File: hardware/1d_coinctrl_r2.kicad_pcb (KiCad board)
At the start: 2 copper layers, 158.8 x 158.8 mm, 99 parts, among them J1 +12V INPUT, J10 USB_B, J2 CO LINE, J3 V_RLY_SEL, J4 TEL LINE, J5 COIN LINE, J6 DB9_Female_MountingHoles, J7 Conn_01x02, J8 Conn_02x10_Odd_Even, J9 Conn_01x06_Male, K1 G5V-2-DC12, K10 L4_COIN_CTRL, K11 G5V-2-DC12, K2 G5V-2-DC12, K3 L1_HOLD, K4 L1_COIN_CTRL, K5 L2_HOLD, K6 L2_COIN_CTRL, K7 L3_HOLD, K8 L3_COIN_CTRL, K9 L4_HOLD, SW1 SW_Push, U10 H11AA1, U14 MAX202, U2 V7805-1000, U3 PIC18F4550-IP, U4 74LS06, U5 74LS06, U6 H11AA1, U7 H11AA1, U8 H11AA1, U9 H11AA1

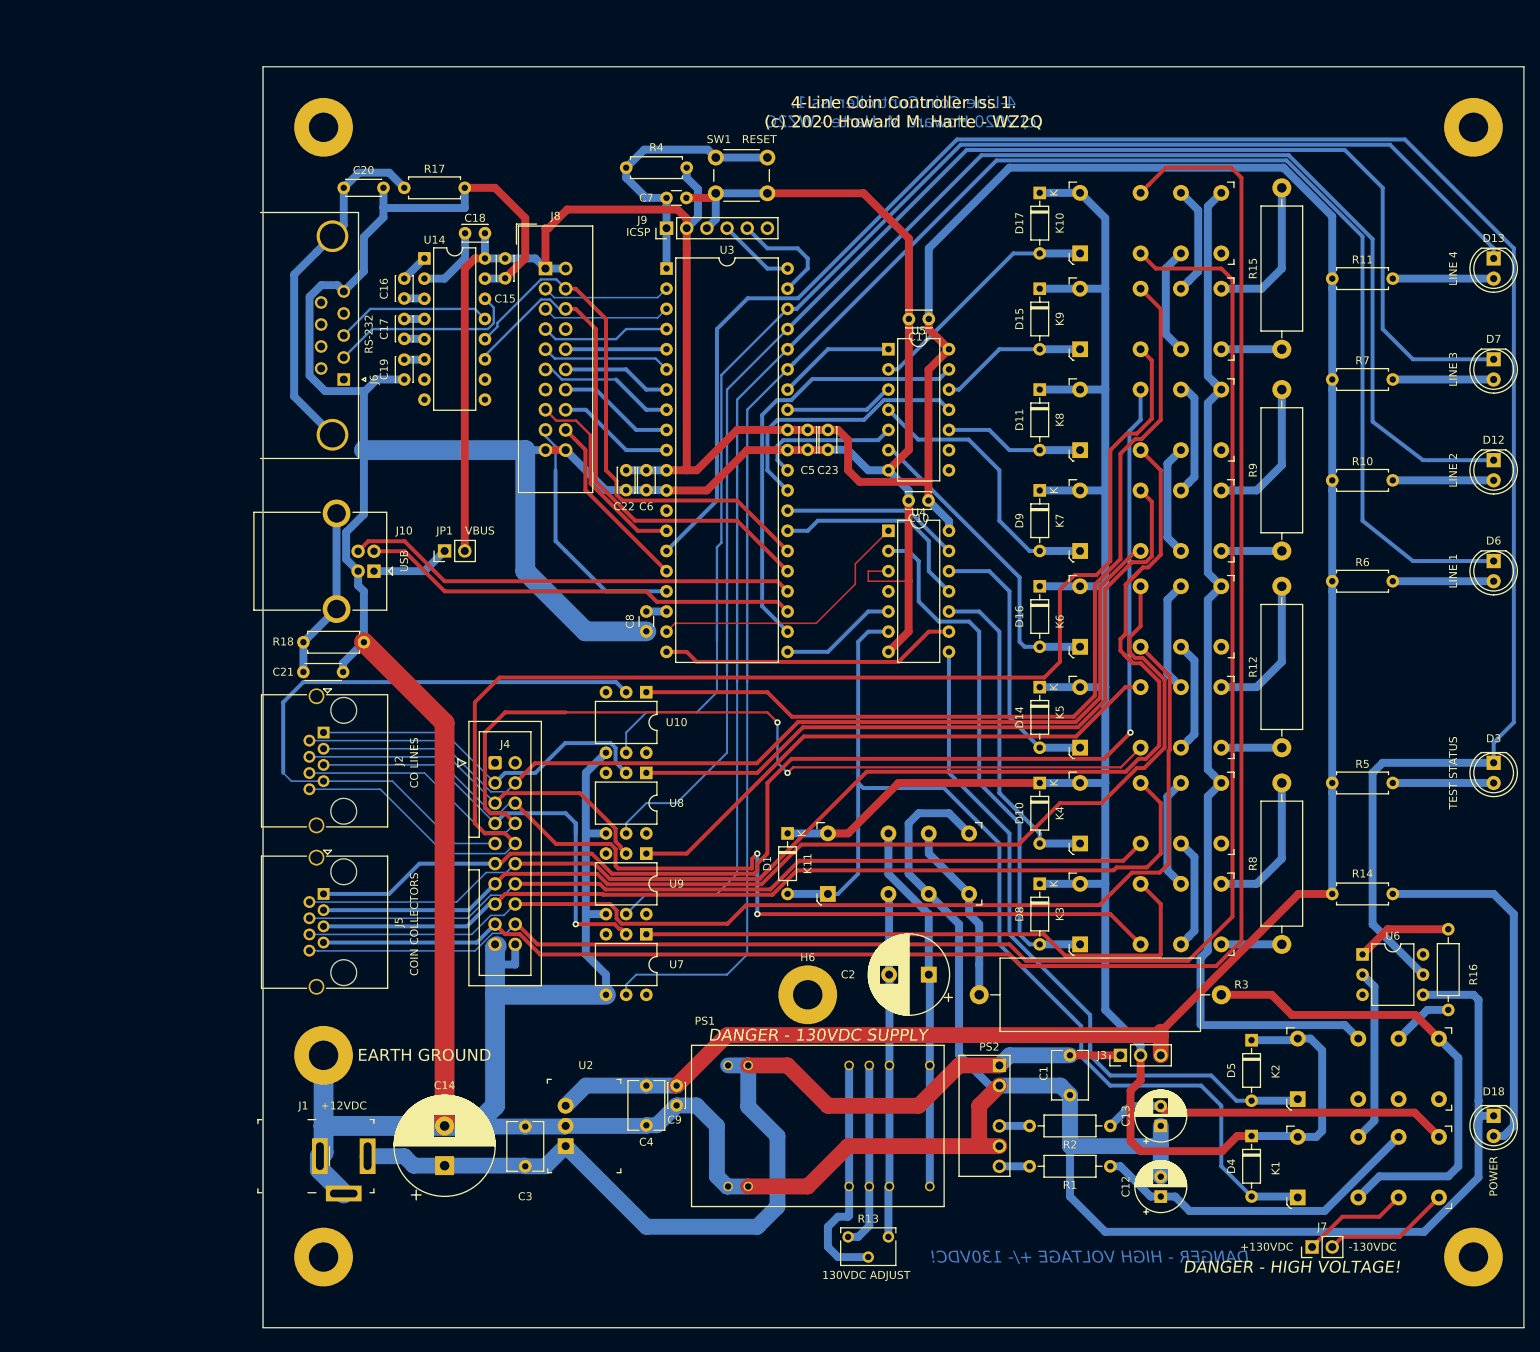
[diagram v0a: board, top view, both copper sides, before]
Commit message: Issue 2 schmatic and Layout
Added polarity reversal detection to monitor answer supervision.
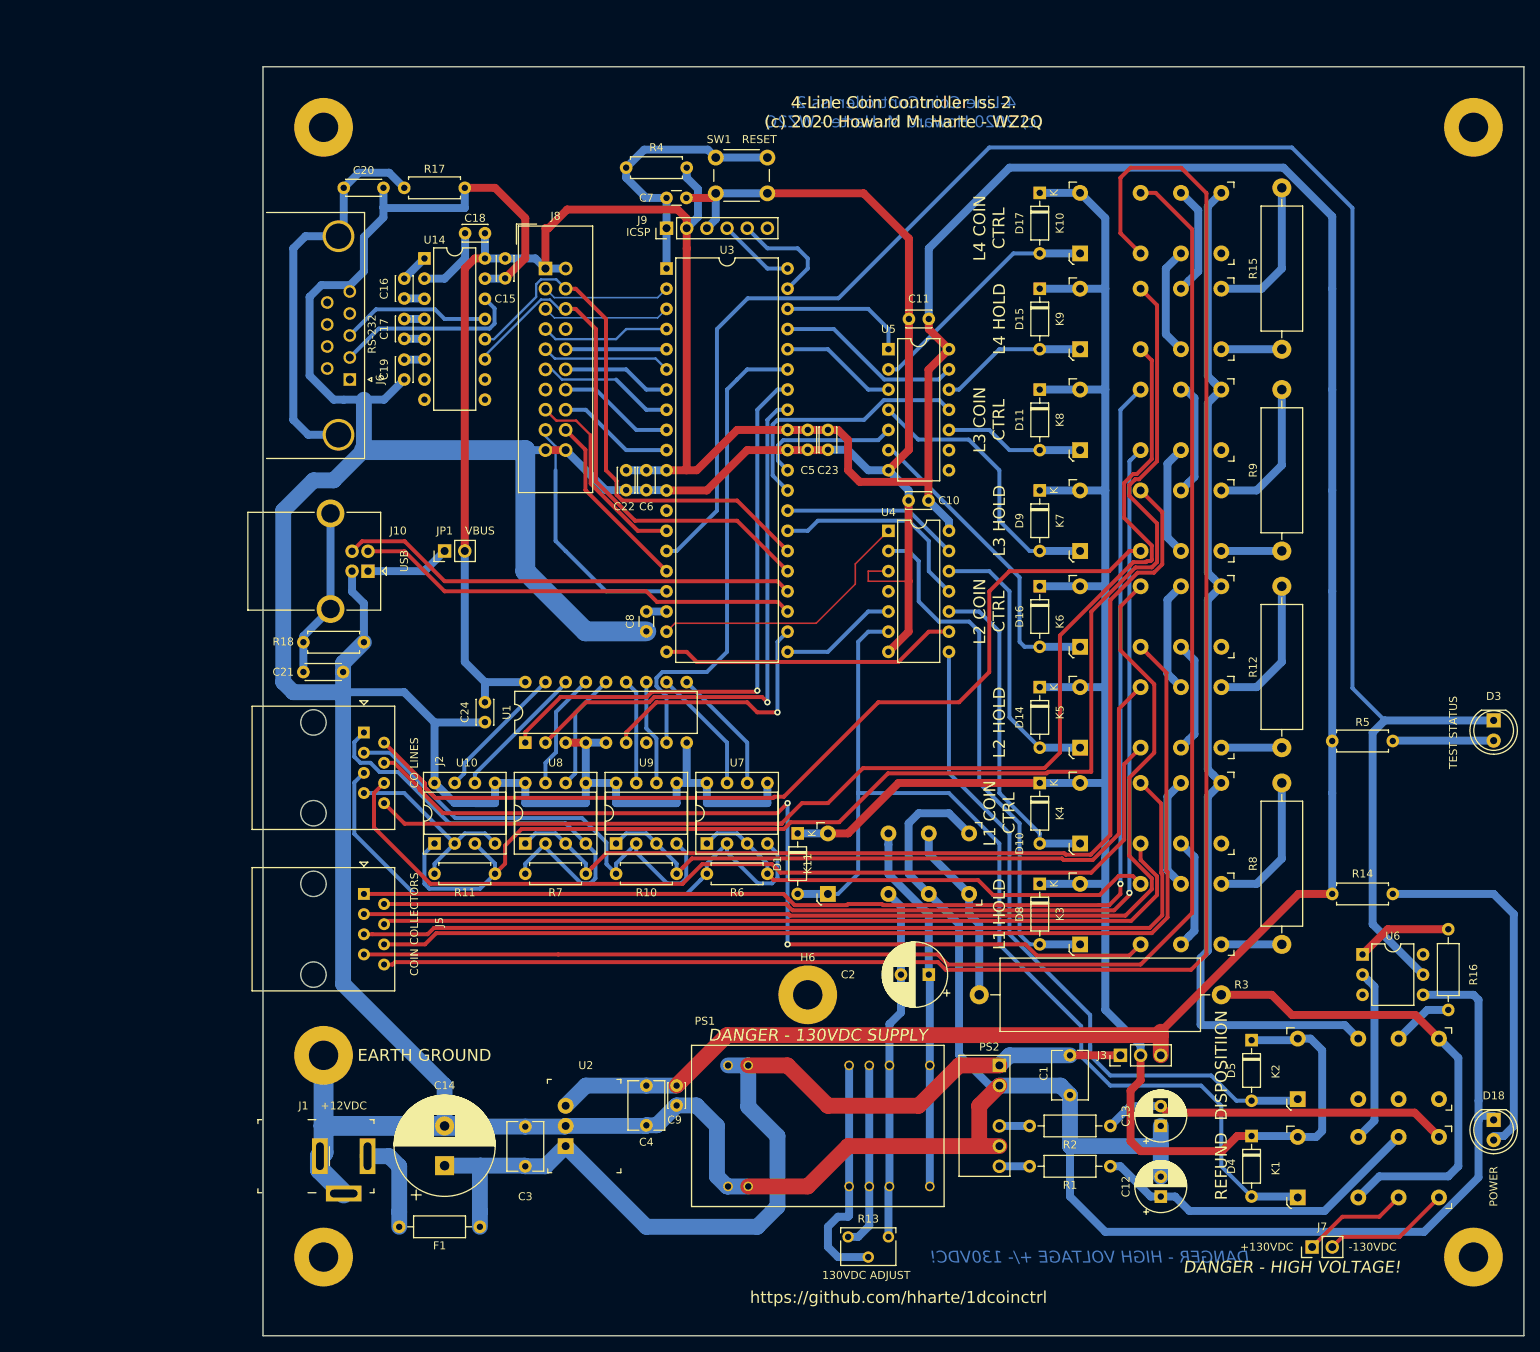
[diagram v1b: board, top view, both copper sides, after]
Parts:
- removed D12, D13, D6, D7: LED, LED_THT:LED_D5.0mm
- removed J4: TEL LINE, Connector_IDC:IDC-Header_2x10_P2.54mm_Vertical
- added C24: 0.1uF, Capacitor_THT:C_Disc_D3.0mm_W2.0mm_P2.50mm, F.Cu at (111.8, 100.3)
- added F1: Fuse, Resistor_THT:R_Axial_DIN0207_L6.3mm_D2.5mm_P10.16mm_Horizontal, F.Cu at (111.1, 166.4)
- added U1: MCP23008-xP, Package_DIP:DIP-18_W7.62mm, F.Cu at (116.8, 105.4)
- C2: footprint Capacitor_THT:CP_Radial_D10.0mm_P5.00mm -> Capacitor_THT:CP_Radial_D8.0mm_P3.50mm
- J2, J5: footprint Connector_RJ:RJ45_Amphenol_RJHSE5380 -> Connector_RJ:RJ45_Amphenol_54602-x08_Horizontal
- R10, R11, R6, R7: value 220 -> 120
- U10, U7, U8, U9: value H11AA1 -> ILD74; footprint Package_DIP:DIP-6_W7.62mm -> Package_DIP:DIP-8_W7.62mm_Socket
- moved R11 129.3 mm to (113.0, 121.9), turned to 180 degrees
- moved R7 112.7 mm to (124.5, 121.9), turned to 180 degrees
- moved R10 96.3 mm to (135.9, 121.9), turned to 180 degrees
- moved R6 80.1 mm to (147.3, 121.9), turned to 180 degrees
- moved U10 32.8 mm to (105.4, 118.1), turned to 90 degrees
- moved U8 17.6 mm to (116.8, 118.1), turned to 90 degrees
- moved U7 13.7 mm to (139.7, 118.1), turned to 90 degrees
- moved D3 5.33 mm to (238.8, 102.6)
- moved R5 5.28 mm to (218.4, 105.2)
- moved J2 5.08 mm to (96.5, 104.1)
- moved J5 5.08 mm to (96.5, 124.5)
- moved U9 4.02 mm to (128.3, 118.1), turned to 90 degrees
- moved D1 1.27 mm to (151.1, 116.8)
- moved J10 0.76 mm to (97.0, 83.8)
- moved J6 0.76 mm to (94.7, 59.7)
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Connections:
- net /GPIO/RD3_DISPOSITION renamed /GPIO/RD1_DISPOSITION
- net /GPIO/RE0_L3_COIN_CONTROL renamed /GPIO/RD6_L3_COIN_CONTROL
- J1 pad 1: +12V -> Net-(F1-Pad2)
- J6 pad 1: Net-(J6-Pad1) -> (no net)
- J6 pad 4: Net-(J6-Pad4) -> (no net)
- J6 pad 6: Net-(J6-Pad6) -> (no net)
- J6 pad 7: Net-(J6-Pad7) -> (no net)
- J6 pad 8: Net-(J6-Pad8) -> (no net)
- J6 pad 9: Net-(J6-Pad9) -> (no net)
- J8 pad 13: Net-(J8-Pad13) -> (no net)
- J8 pad 8: Net-(J8-Pad8) -> (no net)
- J9 pad 6: Net-(J9-Pad6) -> (no net)
- K10 pad 8: Net-(K10-Pad8) -> (no net)
- K2 pad 4: Net-(K2-Pad4) -> (no net)
- K2 pad 6: Net-(K2-Pad6) -> (no net)
- K2 pad 8: Net-(K2-Pad8) -> (no net)
- K4 pad 8: Net-(K4-Pad8) -> (no net)
- K6 pad 8: Net-(K6-Pad8) -> (no net)
- K8 pad 8: Net-(K8-Pad8) -> (no net)
- R10 pad 1: +5V -> Net-(K5-Pad13)
- R10 pad 2: Net-(D12-Pad2) -> /L2_CO_TIP
- R11 pad 1: +5V -> Net-(K9-Pad13)
- R11 pad 2: Net-(D13-Pad2) -> /L4_CO_TIP
- R6 pad 1: +5V -> Net-(K3-Pad13)
- R6 pad 2: Net-(D6-Pad2) -> /L1_CO_TIP
- R7 pad 1: +5V -> Net-(K7-Pad13)
- R7 pad 2: Net-(D7-Pad2) -> /L3_CO_TIP
- U10 pad 3: Net-(U10-Pad3) -> Net-(K9-Pad13)
- U10 pad 4: GND -> /L4_CO_TIP
- U10 pad 5: /GPIO/L4_OFF_HOOK -> GND
- U10 pad 6: Net-(U10-Pad6) -> /Coin Line Control/L4_OFF_HOOK_F
- U14 pad 10: Net-(U14-Pad10) -> (no net)
- U14 pad 7: Net-(U14-Pad7) -> (no net)
- U14 pad 8: Net-(U14-Pad8) -> (no net)
- U14 pad 9: Net-(U14-Pad9) -> (no net)
- U3 pad 13: Net-(U3-Pad13) -> (no net)
- U3 pad 22: /GPIO/RD6_L4_HOLD_CO -> /GPIO/I2C_RESET
- U3 pad 33: /GPIO/RB0_L3_HOLD_CO -> /GPIO/I2C_SDA
- U3 pad 34: /GPIO/RB1_L4_COIN_CONTROL -> /GPIO/I2C_SCL
- U3 pad 35: /GPIO/L1_OFF_HOOK -> /GPIO/I2C_INT
- U3 pad 36: /GPIO/L2_OFF_HOOK -> /GPIO/RB3_L3_HOLD_CO
- U3 pad 37: /GPIO/L3_OFF_HOOK -> /GPIO/RB4_L4_HOLD_CO
- U3 pad 38: /GPIO/L4_OFF_HOOK -> /GPIO/RB1_L4_COIN_CONTROL
- U4 pad 4: Net-(U4-Pad4) -> (no net)
- U5 pad 13: /GPIO/RD6_L4_HOLD_CO -> /GPIO/RB4_L4_HOLD_CO
- U5 pad 3: /GPIO/RB0_L3_HOLD_CO -> /GPIO/RB3_L3_HOLD_CO
- U6 pad 3: Net-(U6-Pad3) -> (no net)
- U6 pad 6: Net-(U6-Pad6) -> (no net)
- U7 pad 3: Net-(U7-Pad3) -> Net-(K3-Pad13)
- U7 pad 4: GND -> /L1_CO_TIP
- U7 pad 5: /GPIO/L1_OFF_HOOK -> GND
- U7 pad 6: Net-(U7-Pad6) -> /Coin Line Control/L1_OFF_HOOK_F
- U8 pad 3: Net-(U8-Pad3) -> Net-(K7-Pad13)
- U8 pad 4: GND -> /L3_CO_TIP
- U8 pad 5: /GPIO/L3_OFF_HOOK -> GND
- U8 pad 6: Net-(U8-Pad6) -> /Coin Line Control/L3_OFF_HOOK_F
- U9 pad 3: Net-(U9-Pad3) -> Net-(K5-Pad13)
- U9 pad 4: GND -> /L2_CO_TIP
- U9 pad 5: /GPIO/L2_OFF_HOOK -> GND
- U9 pad 6: Net-(U9-Pad6) -> /Coin Line Control/L2_OFF_HOOK_F
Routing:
- net /GPIO/L1_OFF_HOOK: track 235.2 -> 0.00 mm
- net /GPIO/L2_OFF_HOOK: track 212.8 -> 0.00 mm
- net /GPIO/L3_OFF_HOOK: track 193.7 -> 0.00 mm
- net /GPIO/L4_OFF_HOOK: track 172.2 -> 0.00 mm
- net /GPIO/I2C_SCL: track 0.00 -> 73.2 mm, vias 0 -> 1
- net /GPIO/I2C_SDA: track 0.00 -> 69.2 mm, vias 0 -> 1
- net /GPIO/I2C_INT: track 0.00 -> 60.6 mm
- net /L4_CO_TIP: track 84.0 -> 25.1 mm
- net Net-(K9-Pad13): track 115.0 -> 171.6 mm
- net /GPIO/RD6_L4_HOLD_CO: track 54.5 -> 0.00 mm
- net GND: track 799.0 -> 839.1 mm
- net Net-(K7-Pad13): track 92.0 -> 127.6 mm
- net /GPIO/I2C_RESET: track 0.00 -> 33.1 mm, vias 0 -> 1
- net /L4_COIN_TIP: track 230.6 -> 202.0 mm
- net +5V: track 454.8 -> 480.0 mm
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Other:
- board size 158.8 x 158.8 mm -> 158.8 x 159.8 mm
- board text added: "4-Line Coin Controller Iss 2. (c) 2020 Howard M. Harte - WZ2Q"
- board text added: "DISPOSITIION"
- board text added: "L1 COIN CTRL"
- board text added: "L1 HOLD"
- board text added: "L2 COIN CTRL"
- board text added: "L2 HOLD"
- board text added: "L3 COIN CTRL"
- board text added: "L3 HOLD"
- board text added: "L4 COIN CTRL"
- board text added: "L4 HOLD"
- board text added: "REFUND"
- board text added: "https://github.com/hharte/1dcoinctrl"
- board text removed: "4-Line Coin Controller Iss 1. (c) 2020 Howard M. Harte - WZ2Q"
- board text removed: "LINE 1"
- board text removed: "LINE 2"
- board text removed: "LINE 3"
- board text removed: "LINE 4"

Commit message: Update for KiCAD 6.06
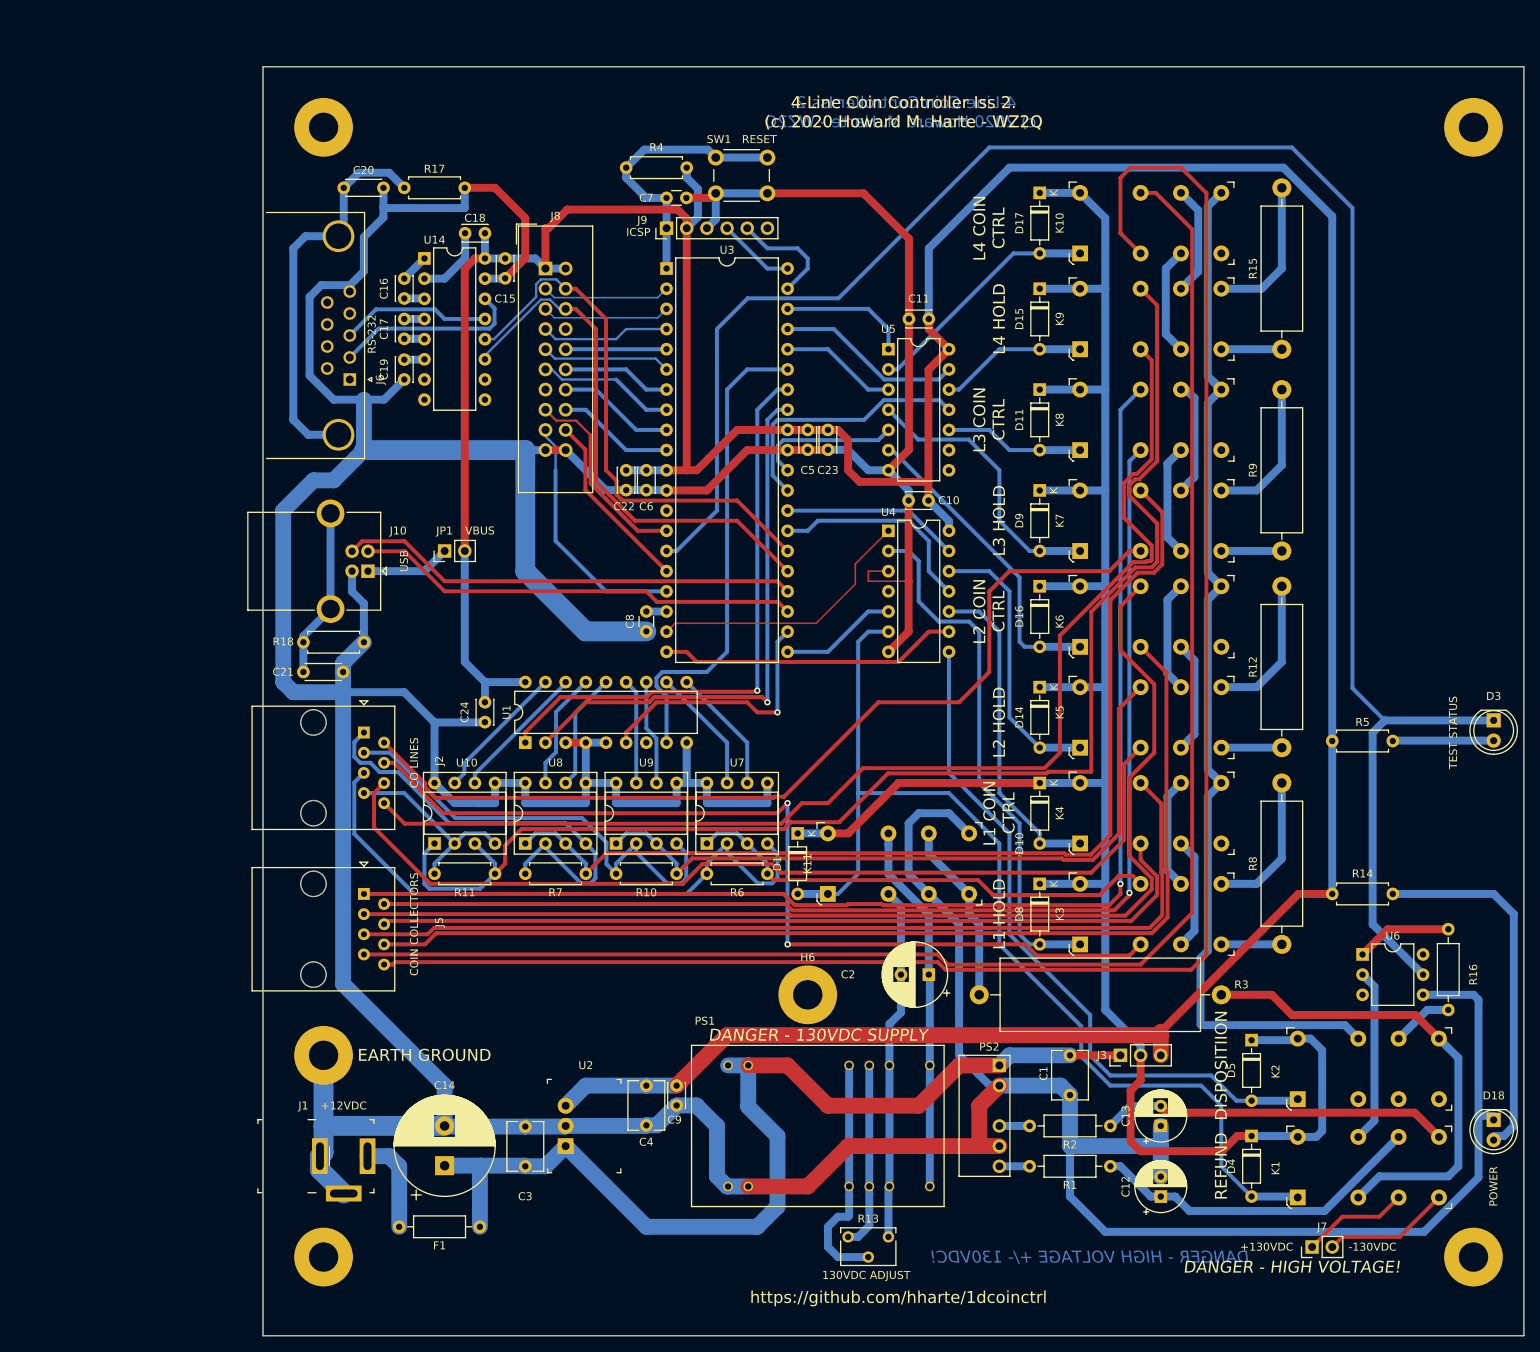
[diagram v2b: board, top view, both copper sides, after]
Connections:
- net /Common Control/+25VDC_TEST renamed /Power/+25VDC
- net /Common Control/-25VDC_TEST renamed /Power/-25VDC
- J6 pad 1: (no net) -> unconnected-(J6-Pad1)
- J6 pad 4: (no net) -> unconnected-(J6-Pad4)
- J6 pad 6: (no net) -> unconnected-(J6-Pad6)
- J6 pad 7: (no net) -> unconnected-(J6-Pad7)
- J6 pad 8: (no net) -> unconnected-(J6-Pad8)
- J6 pad 9: (no net) -> unconnected-(J6-Pad9)
- J8 pad 13: (no net) -> unconnected-(J8-Pad13)
- J8 pad 8: (no net) -> unconnected-(J8-Pad8)
- J9 pad 6: (no net) -> unconnected-(J9-Pad6)
- K10 pad 8: (no net) -> unconnected-(K10-Pad8)
- K2 pad 4: (no net) -> unconnected-(K2-Pad4)
- K2 pad 6: (no net) -> unconnected-(K2-Pad6)
- K2 pad 8: (no net) -> unconnected-(K2-Pad8)
- K4 pad 8: (no net) -> unconnected-(K4-Pad8)
- K6 pad 8: (no net) -> unconnected-(K6-Pad8)
- K8 pad 8: (no net) -> unconnected-(K8-Pad8)
- U1 pad 7: (no net) -> unconnected-(U1-Pad7)
- U14 pad 10: (no net) -> unconnected-(U14-Pad10)
- U14 pad 7: (no net) -> unconnected-(U14-Pad7)
- U14 pad 8: (no net) -> unconnected-(U14-Pad8)
- U14 pad 9: (no net) -> unconnected-(U14-Pad9)
- U3 pad 13: (no net) -> unconnected-(U3-Pad13)
- U4 pad 4: (no net) -> unconnected-(U4-Pad4)
- U6 pad 3: (no net) -> unconnected-(U6-Pad3)
- U6 pad 6: (no net) -> unconnected-(U6-Pad6)
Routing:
- net GND: track 839.1 -> 833.6 mm
- net /Common Control/DISPOSITION: track 88.0 -> 86.7 mm
- net /Power/+130VDC: track 47.7 -> 46.6 mm
- net /L4_CO_RING: track 151.0 -> 150.4 mm
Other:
- net class Default removed
